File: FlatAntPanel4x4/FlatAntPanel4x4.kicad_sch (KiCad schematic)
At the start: 4 parts

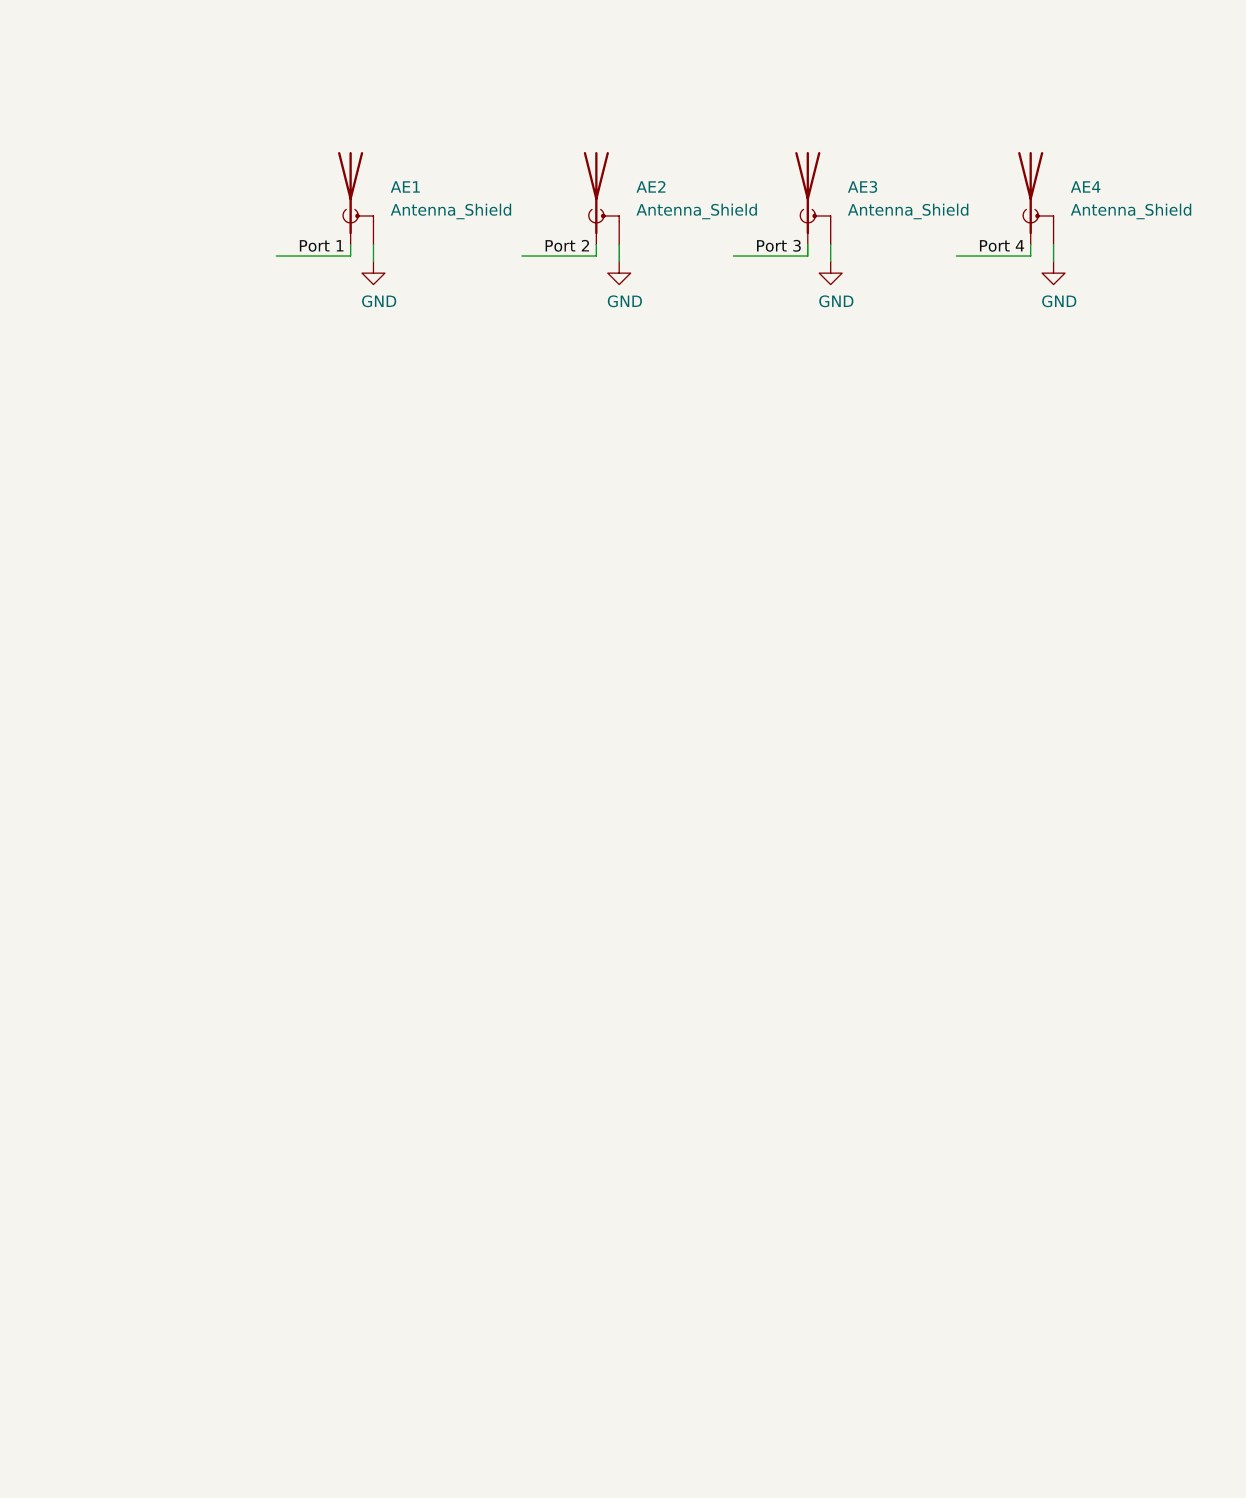
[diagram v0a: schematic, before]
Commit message: Add RF T and angle footprints
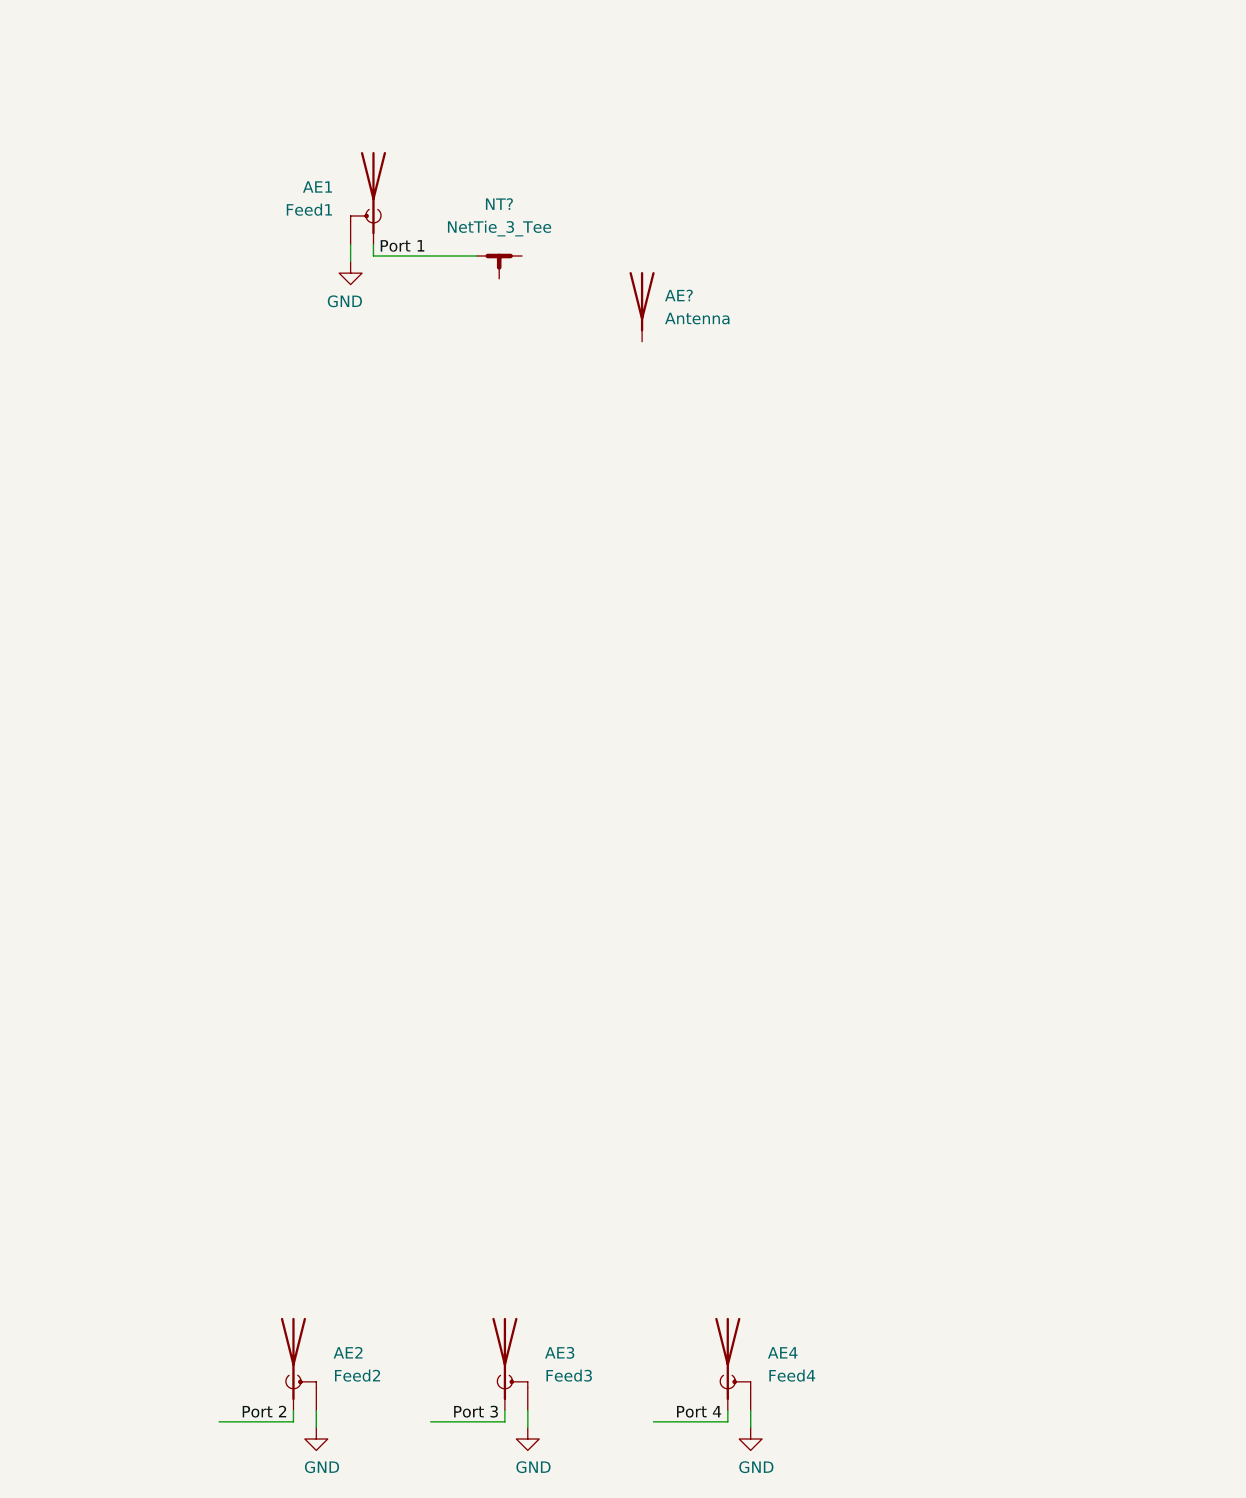
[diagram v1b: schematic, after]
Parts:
- added AE?: Antenna, symbol Device:Antenna
- added NT?: NetTie_3_Tee, Scott:RF-T-50ohm, symbol Device:NetTie_3_Tee
- AE1: value Antenna_Shield -> Feed1
- AE2: value Antenna_Shield -> Feed2
- AE3: value Antenna_Shield -> Feed3
- AE4: value Antenna_Shield -> Feed4
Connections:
- net Port 1: now also NT?.1
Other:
- moved on the sheet: AE1, AE2, AE3, AE4

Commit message: Finish layout of 4x4 panel - bad ground plane yet
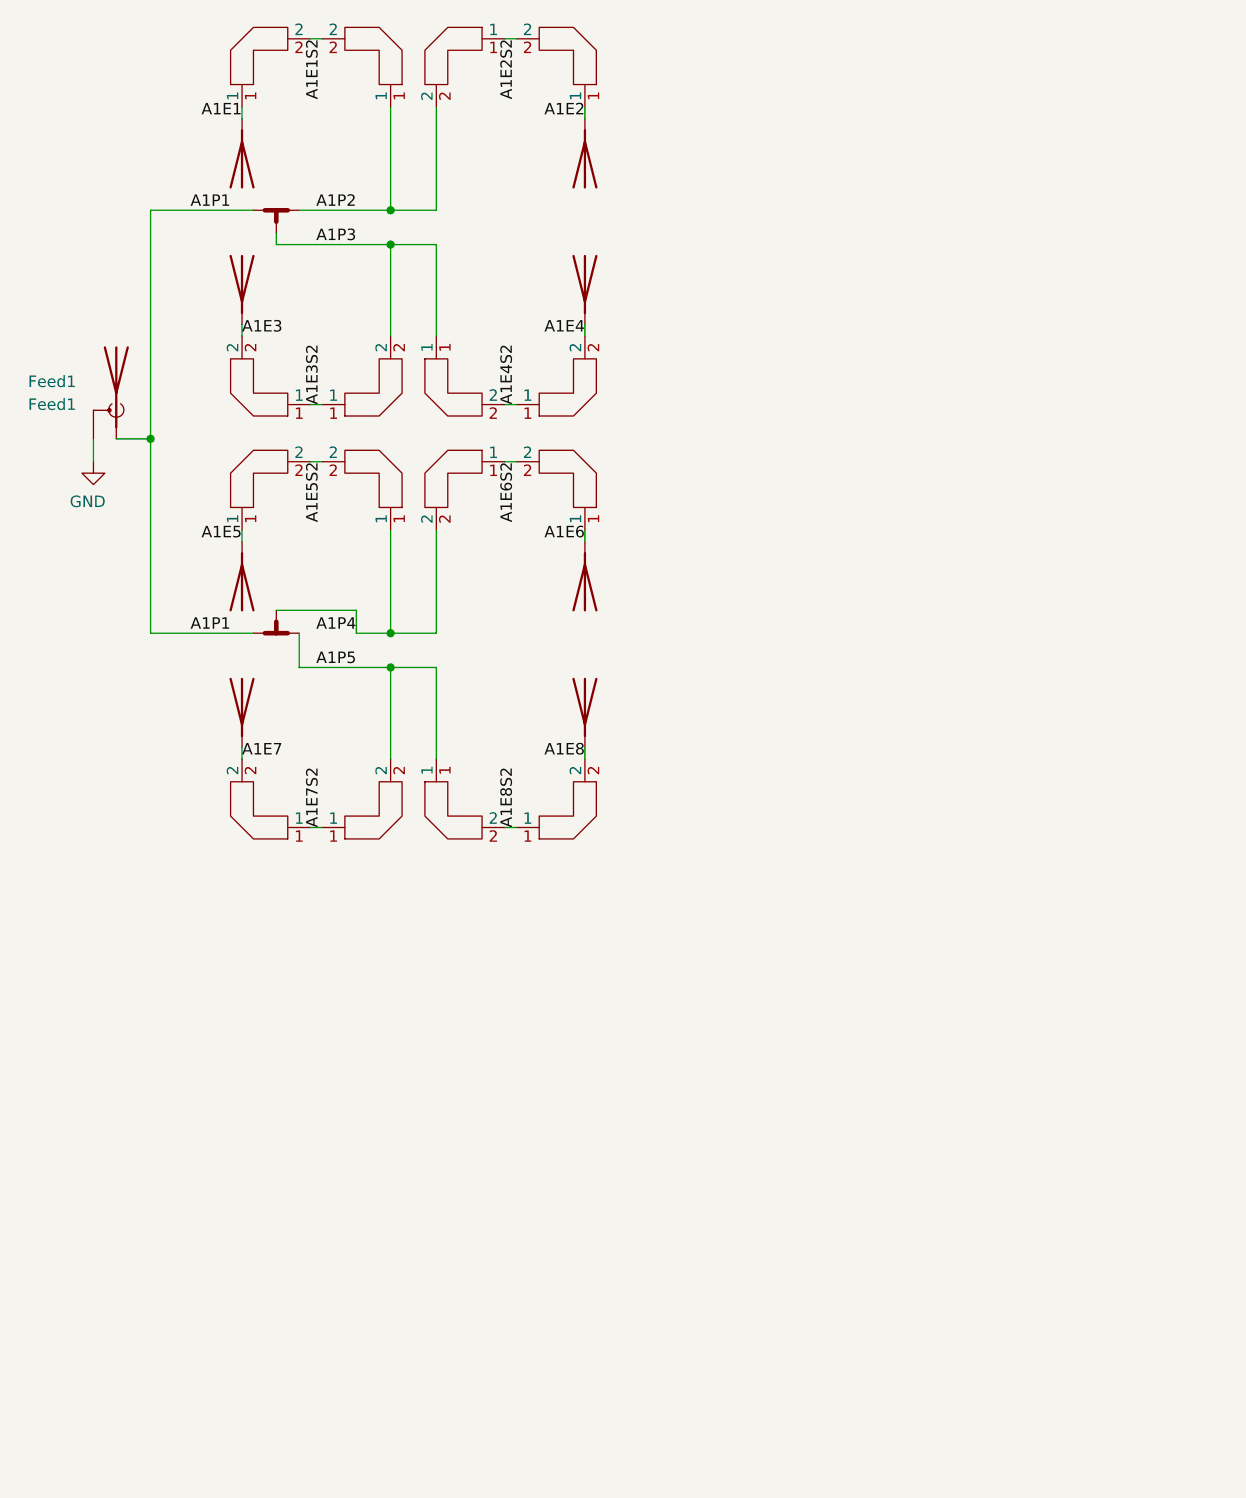
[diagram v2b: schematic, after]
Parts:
- removed AE2: Feed2, symbol Device:Antenna_Shield
- removed AE3: Feed3, symbol Device:Antenna_Shield
- removed AE4: Feed4, symbol Device:Antenna_Shield
- removed AE?: Antenna, symbol Device:Antenna
- added AA1, AA10, AA11, AA12, AA13, AA14, AA15, AA16, AA2, AA3, AA4, AA5, AA6, AA7, AA8, AA9: RFAngle, Scott:RF-Angle-100ohm, symbol Scott:RFAngle
- added AE1, AE2, AE3, AE4, AE5, AE6, AE7, AE8: Antenna, Scott:PanelAnt5.0_V_UP_100R, symbol Device:Antenna
- added NT2: NetTie_3_Tee, Scott:RF-T-50ohm, symbol Device:NetTie_3_Tee
- gave numbers to parts that had none: 1
- renumbered AE1 to Feed1
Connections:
- net A1P2: now reaches NT1.2
- net A1P2: now also AA2.1, AA3.2
- net A1P3: now reaches NT1.3
- net A1P3: now also AA6.2, AA7.1
- net Port 1 renamed A1P1
- net A1P1: now also NT2.1
- new net A1E1: AA1.1, AE1.1 (A)
- new net A1E1S2: AA1.2, AA2.2
- new net A1E2: AA4.1, AE2.1 (A)
- new net A1E2S2: AA3.1, AA4.2
- new net A1E3: AA5.2, AE3.1 (A)
- new net A1E3S2: AA5.1, AA6.1
- new net A1E4: AA8.2, AE4.1 (A)
- new net A1E4S2: AA7.2, AA8.1
- new net A1E5: AA9.1, AE5.1 (A)
- new net A1E5S2: AA10.2, AA9.2
- new net A1E6: AA12.1, AE6.1 (A)
- new net A1E6S2: AA11.1, AA12.2
- new net A1E7: AA13.2, AE7.1 (A)
- new net A1E7S2: AA13.1, AA14.1
- new net A1E8: AA16.2, AE8.1 (A)
- new net A1E8S2: AA15.2, AA16.1
- new net A1P4: AA10.1, AA11.2, NT2.3
- new net A1P5: AA14.2, AA15.1, NT2.2
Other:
- moved on the sheet: Feed1
